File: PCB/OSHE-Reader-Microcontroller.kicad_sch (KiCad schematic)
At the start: 1 part

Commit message: started work adding hierarchical power pins to mcu and sd card sheets
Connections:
- net 3V3: now reaches U4.1 (3V3)
- net GND: now reaches U4.15 (GND)
- net GND: now also U4.17 (GND), U4.28 (GND), U4.31 (GND)
- no-connect marks 0 -> 6
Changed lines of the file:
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@@
 	(generator_version "9.0")
 	(paper "A4")
+	(no_connect
+		(at 104.14 82.55)
+	)
+	(no_connect
+		(at 63.5 52.07)
+	)
+	(no_connect
+		(at 104.14 80.01)
+	)
+	(no_connect
+		(at 104.14 54.61)
+	)
+	(no_connect
+		(at 104.14 52.07)
+	)
+	(no_connect
+		(at 63.5 82.55)
+	)
+	(wire
+		(pts
+			(xy 104.14 77.47) (xy 106.68 77.47)
+		)
+		(stroke
+			(width 0)
+			(type default)
+		)
+	)
+	(wire
+		(pts
+			(xy 104.14 85.09) (xy 106.68 85.09)
+		)
+		(stroke
+			(width 0)
+			(type default)
+		)
+	)
+	(wire
+		(pts
+			(xy 60.96 85.09) (xy 63.5 85.09)
+		)
+		(stroke
+			(width 0)
+			(type default)
+		)
+	)
+	(wire
+		(pts
+			(xy 104.14 49.53) (xy 106.68 49.53)
+		)
+		(stroke
+			(width 0)
+			(type default)
+		)
+	)
+	(wire
+		(pts
+			(xy 60.96 49.53) (xy 63.5 49.53)
+		)
+		(stroke
+			(width 0)
+			(type default)
+		)
+	)
+	(hierarchical_label "GND"
+		(shape input)
+		(at 60.96 85.09 180)
+		(effects
+			(font
+				(size 1.27 1.27)
+			)
+			(justify right)
+		)
+	)
+	(hierarchical_label "3V3"
+		(shape input)
+		(at 60.96 49.53 180)
+		(effects
+			(font
+				(size 1.27 1.27)
+			)
+			(justify right)
+		)
+	)
+	(hierarchical_label "GND"
+		(shape input)
+		(at 106.68 77.47 0)
+		(effects
+			(font
+				(size 1.27 1.27)
+			)
+			(justify left)
+		)
+	)
+	(hierarchical_label "GND"
+		(shape input)
+		(at 106.68 85.09 0)
+		(effects
+			(font
+				(size 1.27 1.27)
+			)
+			(justify left)
+		)
+	)
+	(hierarchical_label "GND"
+		(shape input)
+		(at 106.68 49.53 0)
+		(effects
+			(font
+				(size 1.27 1.27)
+			)
+			(justify left)
+		)
+	)
 	(symbol
 		(lib_id "ESP32-C6-DEV-KIT-N8:ESP32-C6-DEV-KIT-N8")

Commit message: misc work on schematic
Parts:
- U4: footprint (none) -> ESP32-C6-DEV-KIT-N8:ESP32-C6-DEV-KIT-N8
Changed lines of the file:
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@@
 			)
 		)
-		(property "Footprint" ""
+		(property "Footprint" "ESP32-C6-DEV-KIT-N8:ESP32-C6-DEV-KIT-N8"
 			(at 83.82 68.58 0)
 			(effects

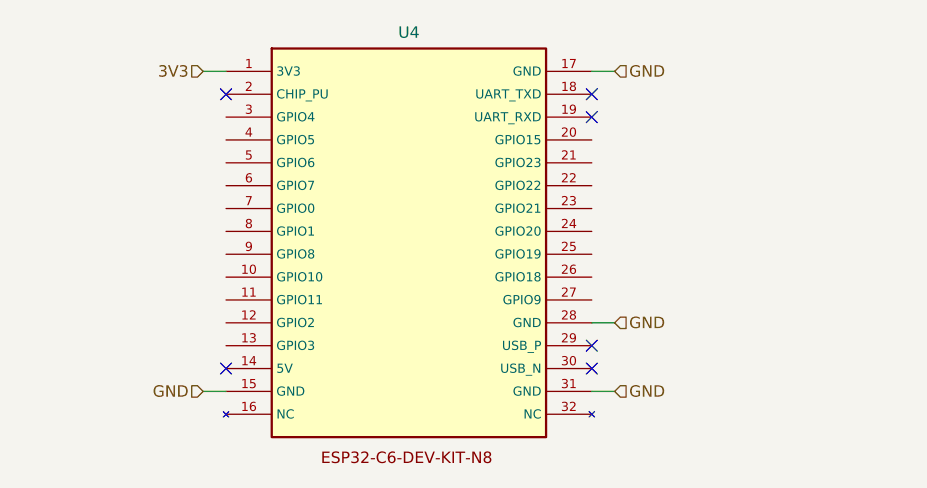
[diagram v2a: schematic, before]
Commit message: cleaned up main sheet and synced labels for presentation
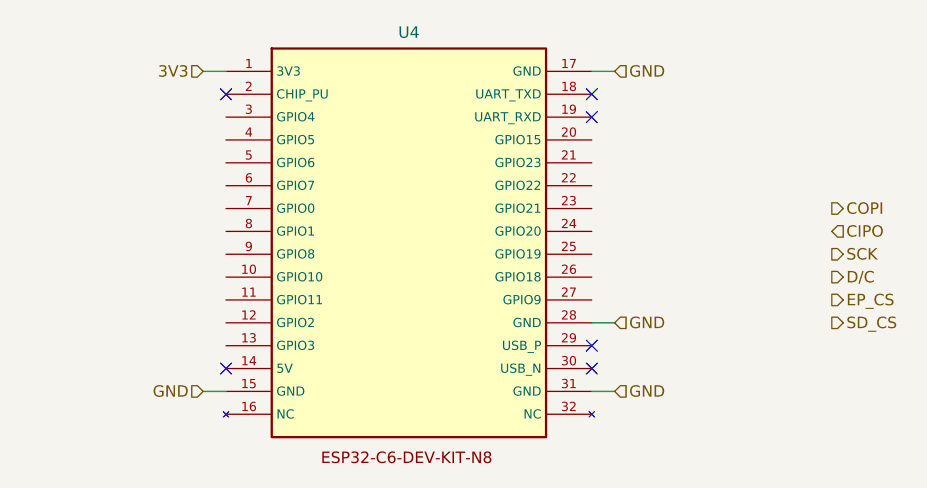
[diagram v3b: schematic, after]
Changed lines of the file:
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@@
+		)
+	)
+	(hierarchical_label "COPI"
+		(shape output)
+		(at 130.81 64.77 0)
+		(effects
+			(font
+				(size 1.27 1.27)
+			)
+			(justify left)
+		)
+	)
+	(hierarchical_label "CIPO"
+		(shape input)
+		(at 130.81 67.31 0)
+		(effects
+			(font
+				(size 1.27 1.27)
+			)
+			(justify left)
 		)
 	)
@@
 		)
 	)
+	(hierarchical_label "D{slash}C"
+		(shape output)
+		(at 130.81 72.39 0)
+		(effects
+			(font
+				(size 1.27 1.27)
+			)
+			(justify left)
+		)
+	)
 	(hierarchical_label "GND"
 		(shape input)
 		(at 106.68 77.47 0)
+		(effects
+			(font
+				(size 1.27 1.27)
+			)
+			(justify left)
+		)
+	)
+	(hierarchical_label "EP_CS"
+		(shape output)
+		(at 130.81 74.93 0)
 		(effects
 			(font
@@
 		)
 	)
+	(hierarchical_label "SD_CS"
+		(shape output)
+		(at 130.81 77.47 0)
+		(effects
+			(font
+				(size 1.27 1.27)
+			)
+			(justify left)
+		)
+	)
 	(hierarchical_label "GND"
 		(shape input)
@@
 		(effects
 			(font
+				(size 1.27 1.27)
+			)
+			(justify left)
+		)
+	)
+	(hierarchical_label "SCK"
+		(shape output)
+		(at 130.81 69.85 0)
+		(effects
+			(font

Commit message: HOPEFULLY GOOD FOR EVER (good for first semester) :)
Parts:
- added C12: 0.1uF, symbol Device:C_Small
- added C13: 10uF, symbol Device:C_Small
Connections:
- net 3V3: now also C12.1, C13.1
- net CIPO: now also U4.12 (GPIO2)
- net COPI: now also U4.6 (GPIO7)
- net EP_CS: now also U4.25 (GPIO19)
- net GND: now also C12.2, C13.2
- net SCK: now also U4.5 (GPIO6)
- net SD_CS: now also U4.26 (GPIO18)
- net UpButton: now reaches U4.10 (GPIO10)
- net DownButton: now reaches U4.11 (GPIO11)
- net EP_RESET: now reaches U4.13 (GPIO3)
- net LeftButton: now reaches U4.21 (GPIO23)
- net RightButton: now reaches U4.22 (GPIO22)
- net HomeButton: now reaches U4.23 (GPIO21)
- net EP_D/C: now reaches U4.24 (GPIO20)
- net BAT+: now reaches U4.7 (GPIO0)
- net BAT_STAT: now reaches U4.8 (GPIO1)
- net EP_BUSY: now reaches U4.9 (GPIO8)
- no-connect marks 6 -> 10

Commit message: small
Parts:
- removed C12: 0.1uF, symbol Device:C_Small
- removed C13: 10uF, symbol Device:C_Small
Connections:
- net CIPO: no longer U4.12 (GPIO2)
- net COPI: no longer U4.6 (GPIO7)
- net EP_CS: no longer U4.25 (GPIO19)
- net SCK: no longer U4.5 (GPIO6)
- net SD_CS: no longer U4.26 (GPIO18)
- net BAT+: no longer names the net of U4.7 (GPIO0)
- net BAT_STAT: no longer names the net of U4.8 (GPIO1)
- net DownButton: no longer names the net of U4.11 (GPIO11)
- net EP_BUSY: no longer names the net of U4.9 (GPIO8)
- net EP_D/C: no longer names the net of U4.24 (GPIO20)
- net EP_RESET: no longer names the net of U4.13 (GPIO3)
- net HomeButton: no longer names the net of U4.23 (GPIO21)
- net LeftButton: no longer names the net of U4.21 (GPIO23)
- net RightButton: no longer names the net of U4.22 (GPIO22)
- net UpButton: no longer names the net of U4.10 (GPIO10)
- no-connect marks 10 -> 6
